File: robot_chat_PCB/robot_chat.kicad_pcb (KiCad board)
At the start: 4 copper layers, 90 x 72 mm, 112 parts, among them IC401 NCS199A3RSQT2G, IC402 NCS199A3RSQT2G, J201 STLink, J301 Bat, J401 L_Mot, J402 R_Mot, J501 Bump, J502 Lidar, J503 B_Detect, J504 F_Detect, J601 BT, SW201 RST, SW301 SW_SPDT_MSM, SW601 Start, SW602 Status, U201 STM32G070RBTx, U301 MP1475DJ-LF-P, U302 MIC5317-3.3xM5, U401 ZXBM5210-SP, U402 ZXBM5210-SP, U501 LSM6DSM, Y201 16MHz

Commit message: Routage final v1.2
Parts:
- F301: value 5A -> 10A; footprint Fuse:Fuse_0603_1608Metric -> Fuse:Fuse_1206_3216Metric
- moved F301 0.60 mm to (115.3, 123.7)
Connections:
- net Net-(D302-K) renamed /Power Supply/BST
- net Net-(D304-K) renamed /Power Supply/PG
- net Net-(IC401-IN+) renamed /Motor drivers/IN_R+
- net Net-(IC401-IN-) renamed /Motor drivers/IN_R-
- net Net-(IC402-IN+) renamed /Motor drivers/IN_L+
- net Net-(IC402-IN-) renamed /Motor drivers/IN_L-
- net Net-(U201-PF0) renamed /STM/QUARTZ_0
- net Net-(U201-PF1) renamed /STM/QUARTZ_1
- net Net-(U201-VREF+) renamed /STM/VREF+
- net Net-(U301-EN/SYNC) renamed /Power Supply/EN/SYNC
- net Net-(U301-FB) renamed /Power Supply/FB
- net Net-(U301-SW) renamed /Power Supply/SW
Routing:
- net /Motor drivers/MOTOR_R-: track 9.60 -> 0.00 mm
- net /Motor drivers/MOTOR_L-: track 10.3 -> 5.21 mm
- net /STM/LIDAR_TX: track 27.9 -> 30.2 mm
- net /STM/LIDAR_RX: track 28.7 -> 30.3 mm
- added copper zone on F.Cu, net /Motor drivers/MOTOR_L-
- added copper zone on F.Cu, net /Motor drivers/MOTOR_R-

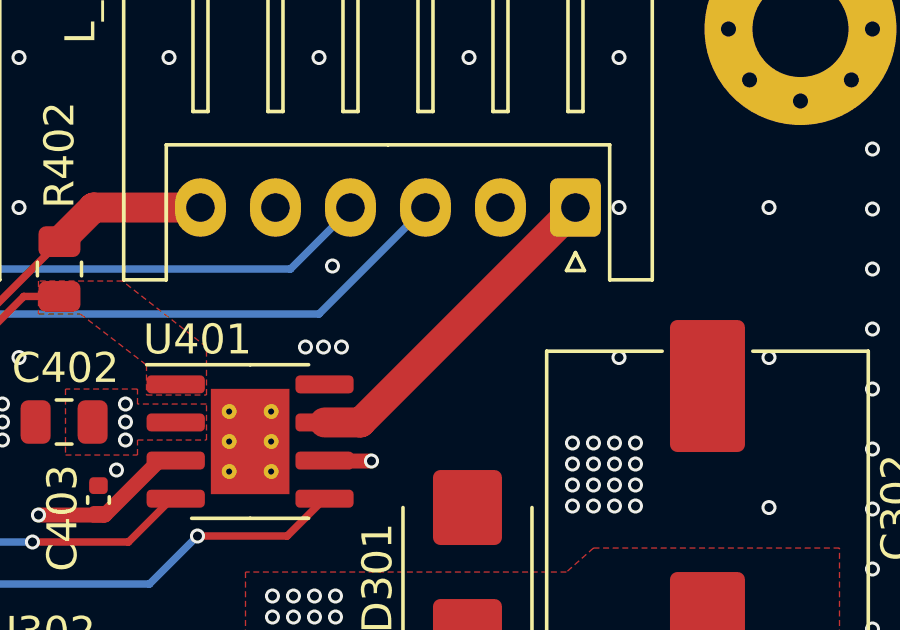
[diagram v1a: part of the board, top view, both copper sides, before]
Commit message: fixed DRC, added html bom
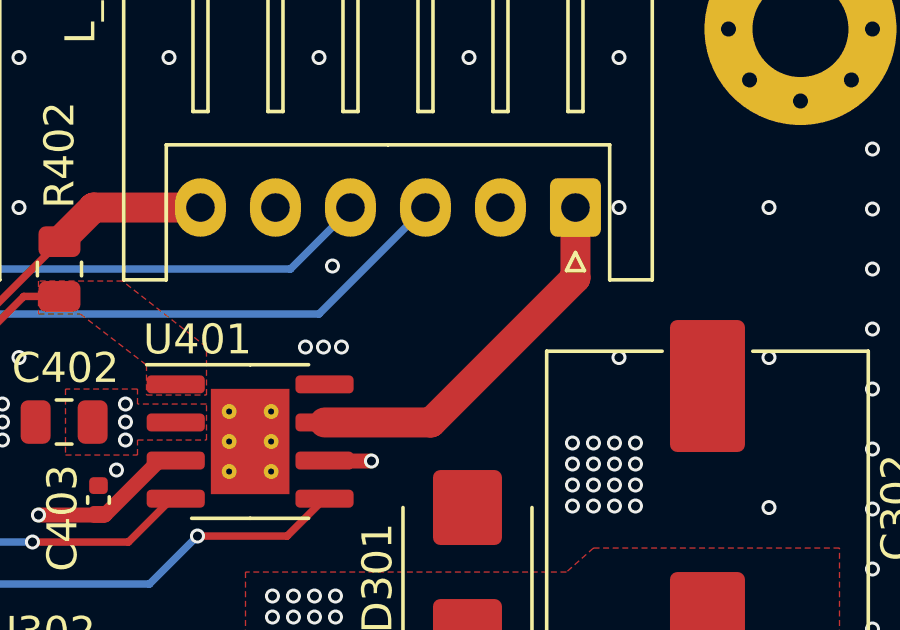
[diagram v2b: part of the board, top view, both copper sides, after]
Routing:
- net /Motor drivers/MOTOR_L+: track 11.3 -> 12.7 mm
